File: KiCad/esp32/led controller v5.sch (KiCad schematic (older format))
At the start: 119 parts, among them J1 Conn_02x15_Counter_Clockwise, J10 Jack-DC, J13 i2c_3.3v, J2 charger, J3 Screw_Terminal_01x09, J4 Screw_Terminal_01x04, J5 Screw_Terminal_01x08, J6 OLED, J7 inverter, J8 i2c_5v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

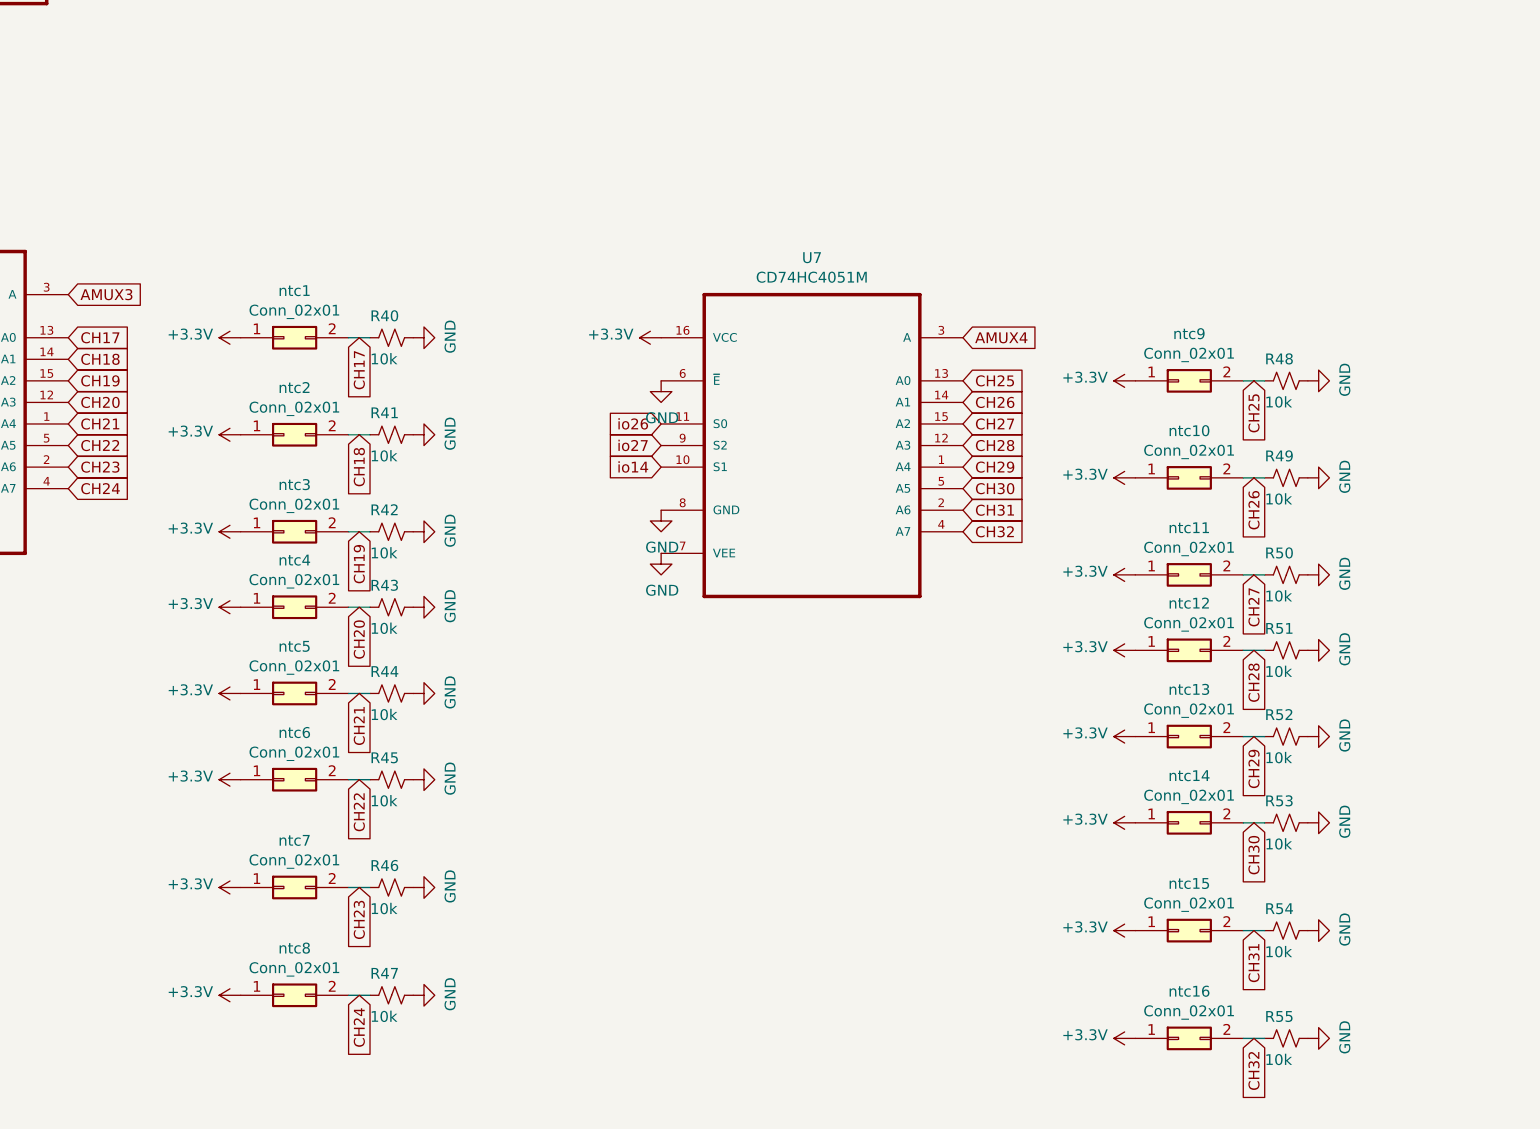
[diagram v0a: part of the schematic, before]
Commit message: updated ESP32 board
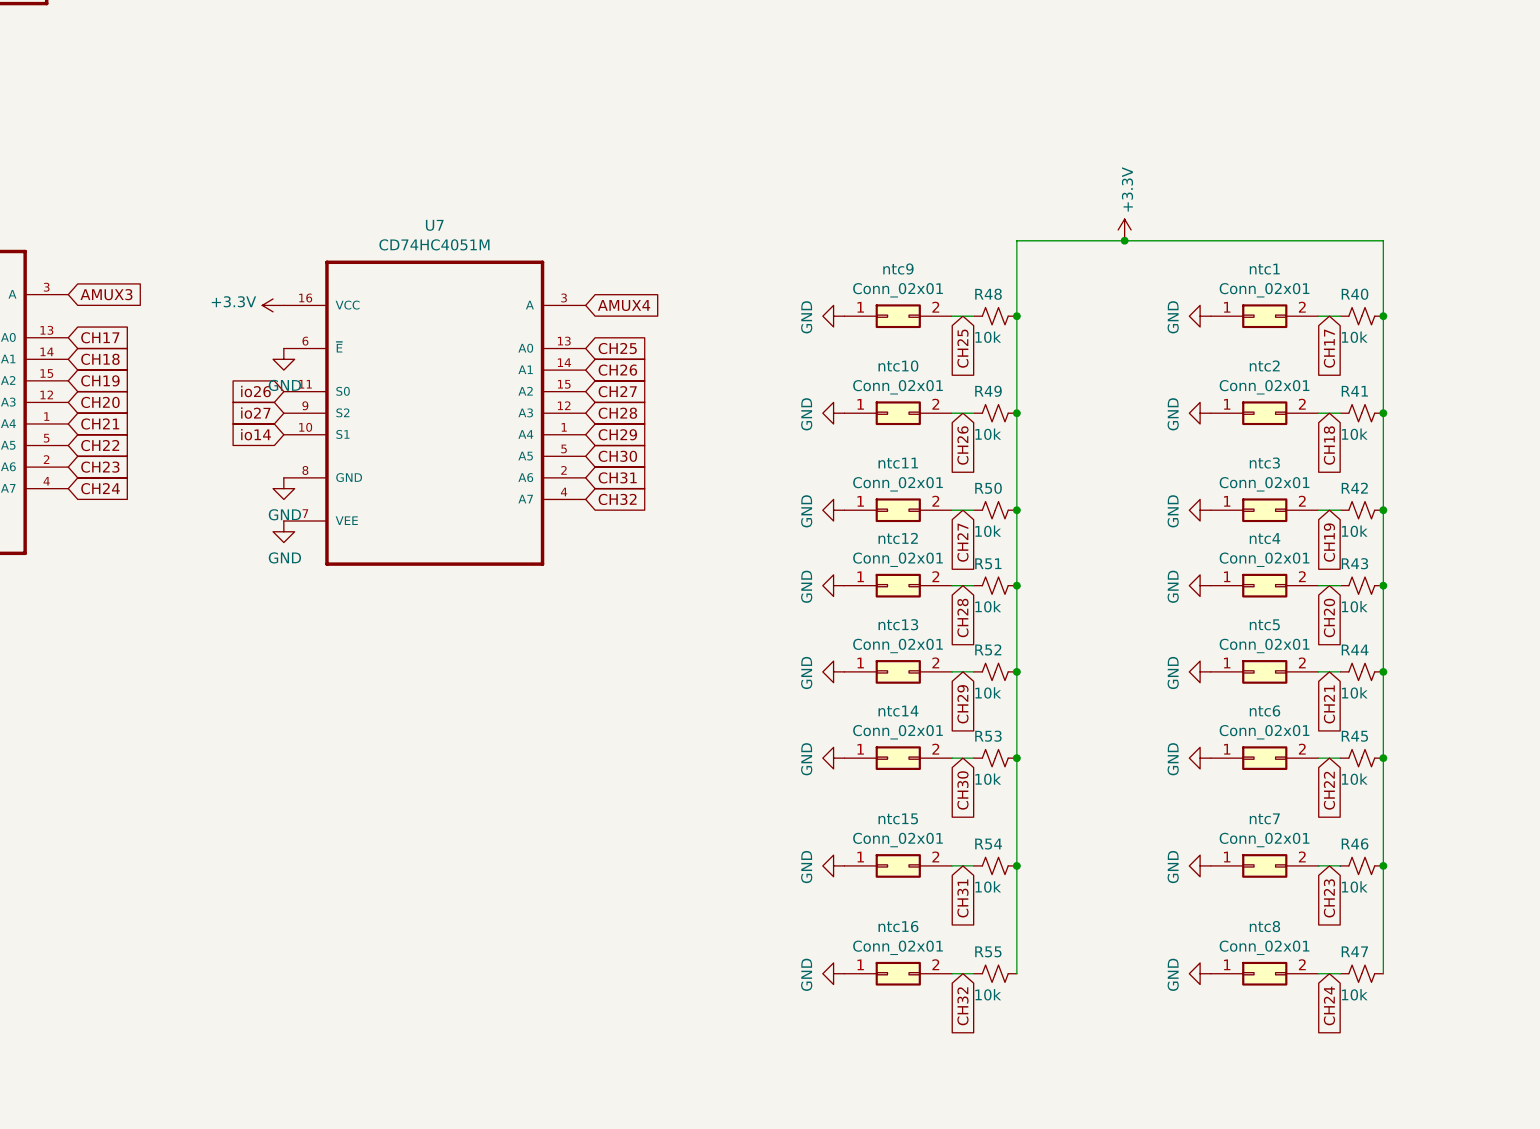
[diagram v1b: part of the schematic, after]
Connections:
- wire segments 78 -> 96
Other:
- moved on the sheet: R40, R41, R42, R43, R44, R45, R46, R47, R48, R49, R50, R51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
